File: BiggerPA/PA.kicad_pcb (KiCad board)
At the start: 2 copper layers, 100 x 100 mm, 129 parts, among them J1 Conn_Coaxial, J10 Conn_01x01, J12 Conn_01x01, J13 Conn_01x01, J14 Conn_01x01, J16 Conn_01x01, J2 Conn_01x02, J27 Conn_01x01, J3 Conn_Coaxial, J4 Conn_01x02, J5 Conn_01x02, J6 Conn_01x01, J7 Conn_01x01, J8 Conn_01x01, J9 Conn_01x01, Q1 2N3906, Q10 IRF510N, Q11 IRF510N, Q14 IRF510N, Q15 IRF510N, Q2 IRF510N, Q3 IRF510N, Q5 2N3906, Q6 IRF510N, Q7 IRF510N, T1 Transformer_1P1Sdotted, T2 Transformer_1P1Sdotted, T3 Transformer_1P1Sdotted, U1 LM7805_TO220

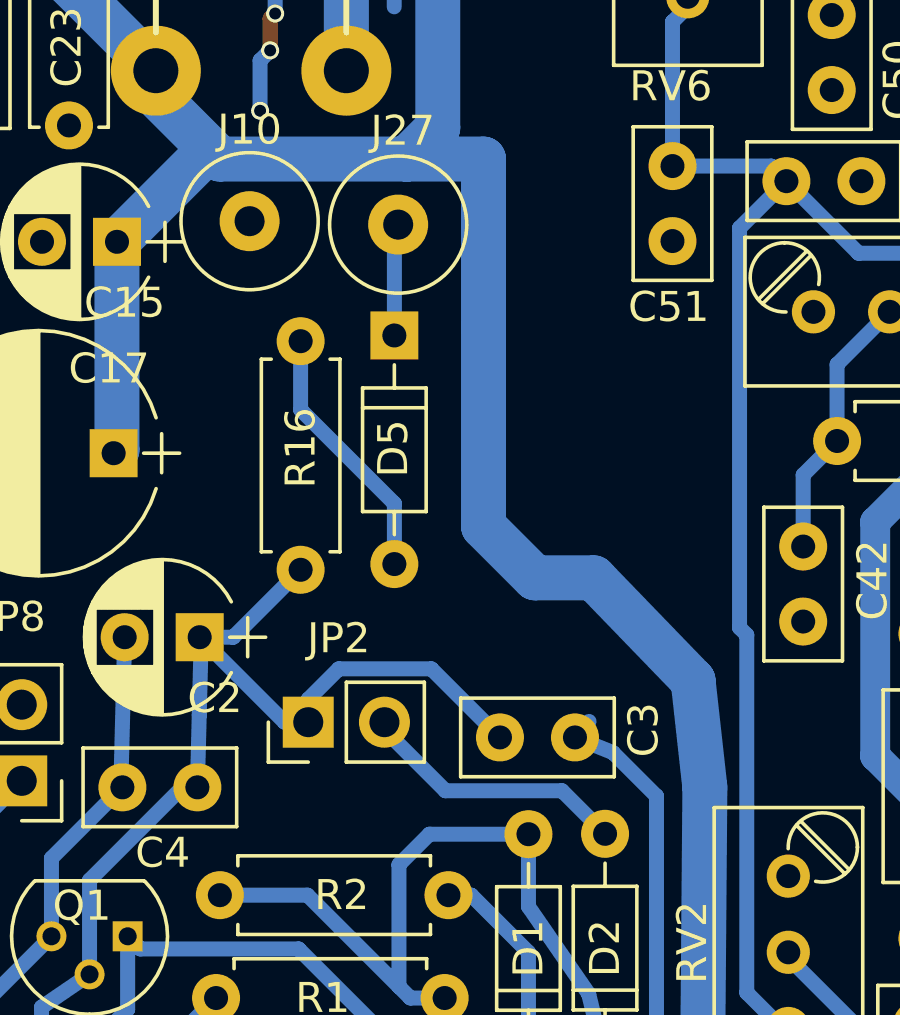
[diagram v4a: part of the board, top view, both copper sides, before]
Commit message: Changed rig RX/TX control
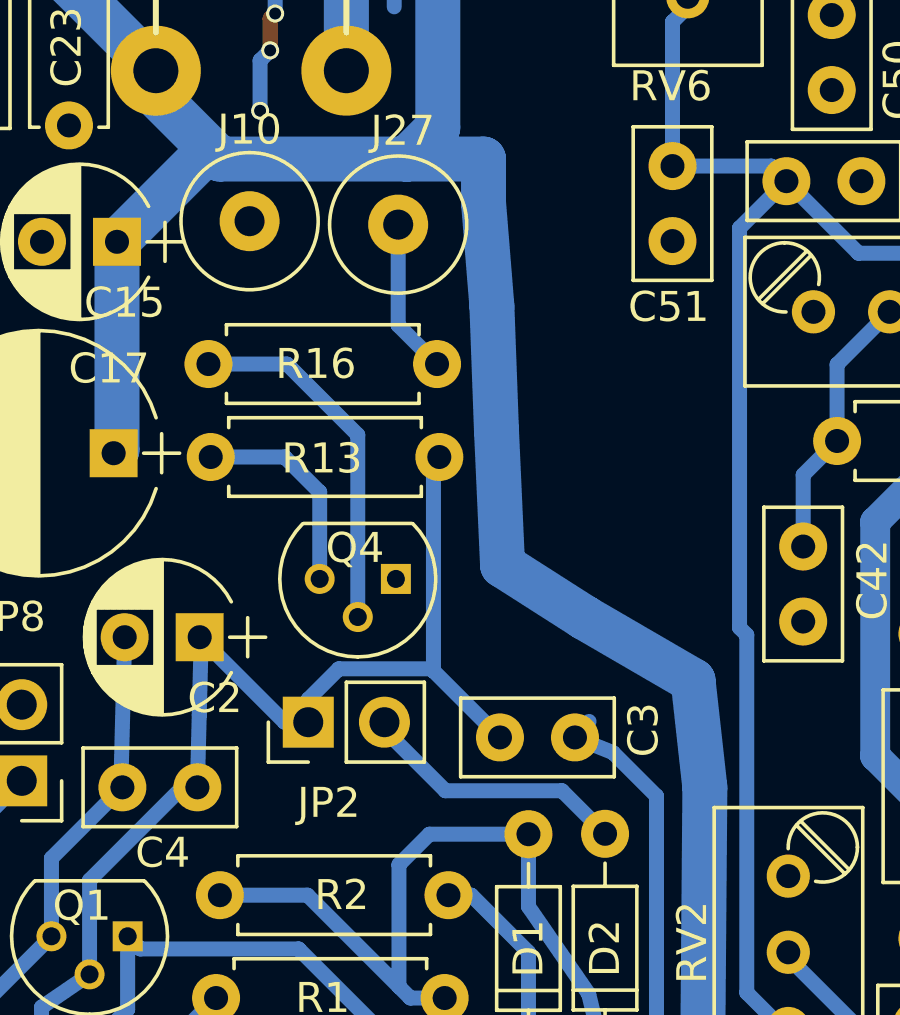
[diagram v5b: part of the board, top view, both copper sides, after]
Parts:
- removed D5: 1N4148, Diodes_THT:D_DO-35_SOD27_P7.62mm_Horizontal
- added Q4: 2N3904, TO_SOT_Packages_THT:TO-92_Molded_Narrow, F.Cu at (113.2, 80.3)
- added R13: 1k, Resistors_THT:R_Axial_DIN0207_L6.3mm_D2.5mm_P7.62mm_Horizontal, F.Cu at (107.0, 76.3)
- R16: value 470R -> 1k
- R35: value 470R -> 100R
- R36, R37, R38, R39, R40, R41: value 4R7 -> 2R2
- moved R16 3.17 mm to (106.9, 73.2), turned to 0 degrees
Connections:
- J27 pad 1: Net-(D5-Pad1) -> Net-(J27-Pad1)
- R16 pad 2: Net-(C2-Pad1) -> Net-(J27-Pad1)
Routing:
- net Net-(Q4-Pad3): track 0.00 -> 7.01 mm
- net Net-(J27-Pad1): track 0.00 -> 5.36 mm
- net Net-(D5-Pad1): track 3.75 -> 0.00 mm
- net Net-(Q4-Pad2): track 8.72 -> 12.0 mm
- net Net-(C2-Pad1): track 44.2 -> 47.2 mm

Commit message: Fixed polarity of rig RXTX relay grounding
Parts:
- removed Q4: 2N3904, TO_SOT_Packages_THT:TO-92_Molded_Narrow
- R13: value 1k -> 10k
- R16: value 1k -> 100k
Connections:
- R13 pad 1: Net-(Q4-Pad3) -> Net-(J27-Pad1)
- R16 pad 1: Net-(Q4-Pad2) -> GND
- R16 pad 2: Net-(J27-Pad1) -> Net-(C2-Pad1)
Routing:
- net Net-(Q4-Pad2): track 12.0 -> 0.00 mm
- net Net-(Q4-Pad3): track 7.01 -> 0.00 mm
- net Net-(J27-Pad1): track 5.36 -> 10.5 mm
- net Net-(C2-Pad1): track 47.2 -> 50.3 mm

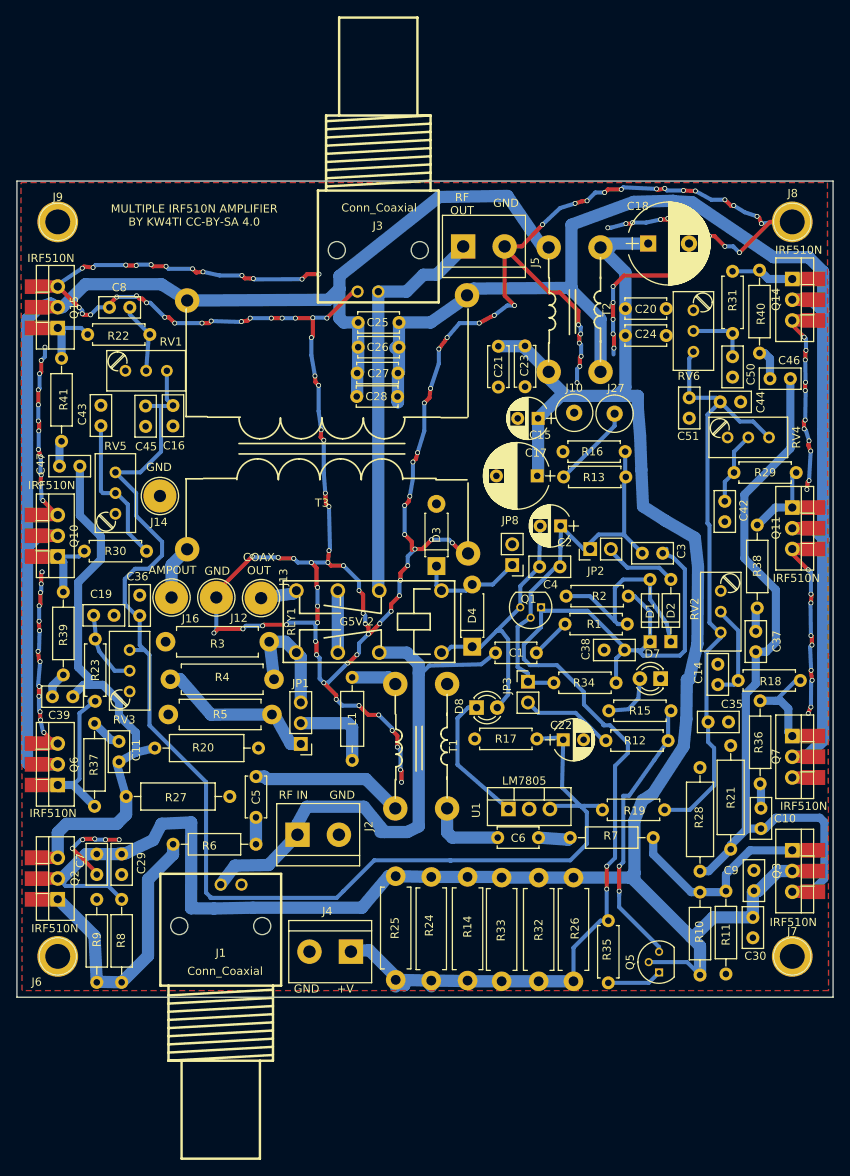
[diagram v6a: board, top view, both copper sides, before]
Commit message: Moved series resistor closer to common drain amplifier to prevent oscillation
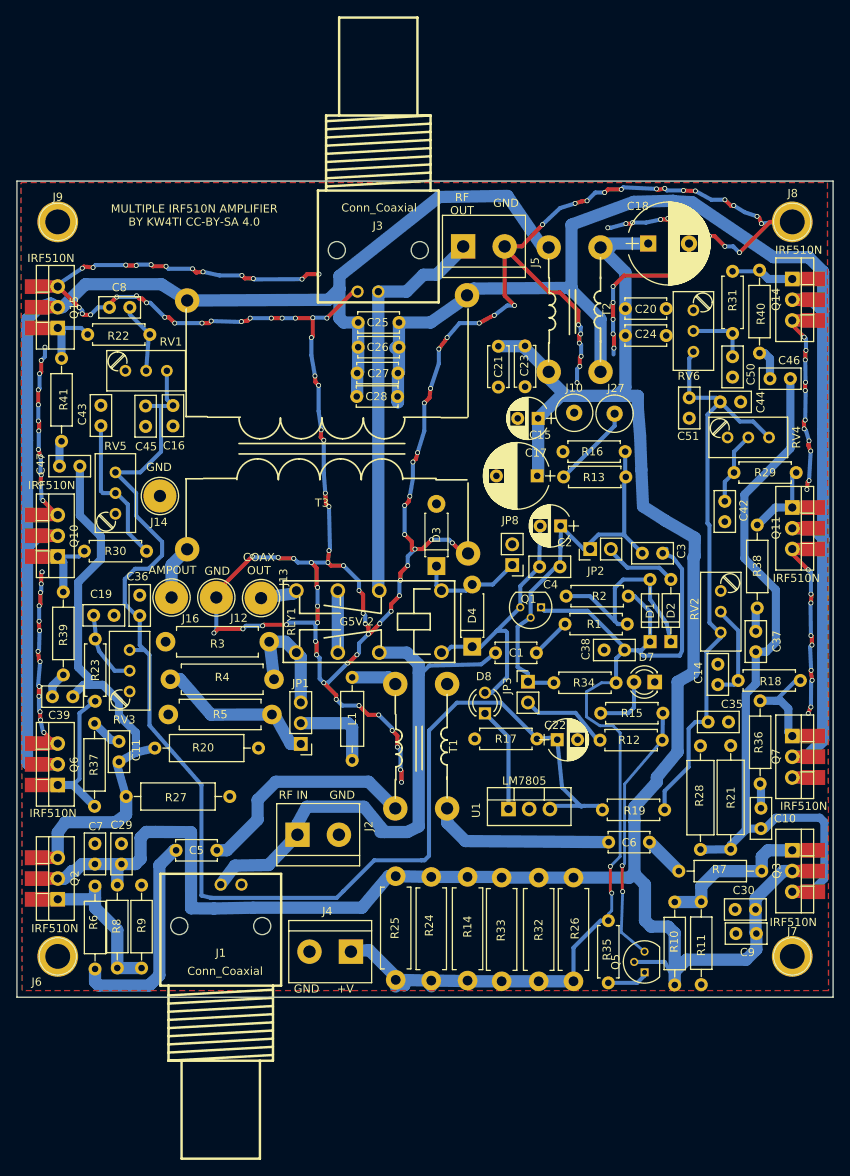
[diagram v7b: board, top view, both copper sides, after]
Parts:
- moved R6 24.9 mm to (49.6, 136.5), turned to 90 degrees
- moved R7 13.9 mm to (121.1, 124.5)
- moved C6 13.6 mm to (112.5, 121.0)
- moved C5 10.6 mm to (59.5, 122.0), turned to 0 degrees
- moved R9 5.76 mm to (55.3, 136.4)
- moved C30 5.31 mm to (128.0, 129.2), turned to 0 degrees
- moved C7 3.78 mm to (49.6, 121.2), turned to 270 degrees
- moved C29 3.78 mm to (52.8, 121.2), turned to 270 degrees
- moved R10 3.33 mm to (120.6, 138.5)
- moved R11 3.29 mm to (123.8, 128.3)
- moved R28 2.66 mm to (123.8, 121.9)
- moved C9 2.14 mm to (128.1, 132.2), turned to 0 degrees
- moved R8 1.83 mm to (52.3, 126.3)
- moved Q5 1.78 mm to (116.9, 136.9)
- moved D8 1.26 mm to (97.3, 105.2), turned to 90 degrees
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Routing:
- net Net-(C5-Pad1): track 3.30 -> 26.5 mm
- net Net-(Q2-Pad1): track 37.2 -> 21.4 mm
- net Net-(C6-Pad1): track 9.99 -> 23.1 mm
- net +12V: track 140.3 -> 127.6 mm
- net GND: track 483.2 -> 472.5 mm, vias 170 -> 165
- net Net-(C5-Pad2): track 18.7 -> 28.1 mm
- net +5V: track 158.1 -> 164.4 mm
- net Net-(Q3-Pad1): track 27.0 -> 22.1 mm
- net Net-(D8-Pad1): track 16.8 -> 12.9 mm
- net PASUPPLY: track 269.2 -> 266.5 mm
- net Net-(Q5-Pad3): track 34.6 -> 32.9 mm
- net Net-(Q5-Pad1): track 6.75 -> 5.21 mm
- net Net-(C35-Pad1): track 75.3 -> 73.8 mm
- net Net-(C10-Pad2): track 94.3 -> 93.1 mm
- net Net-(C6-Pad2): track 4.00 -> 5.07 mm
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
